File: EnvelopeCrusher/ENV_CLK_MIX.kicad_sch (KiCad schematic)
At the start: 12 parts, among them U14 TL072, U6 TL072

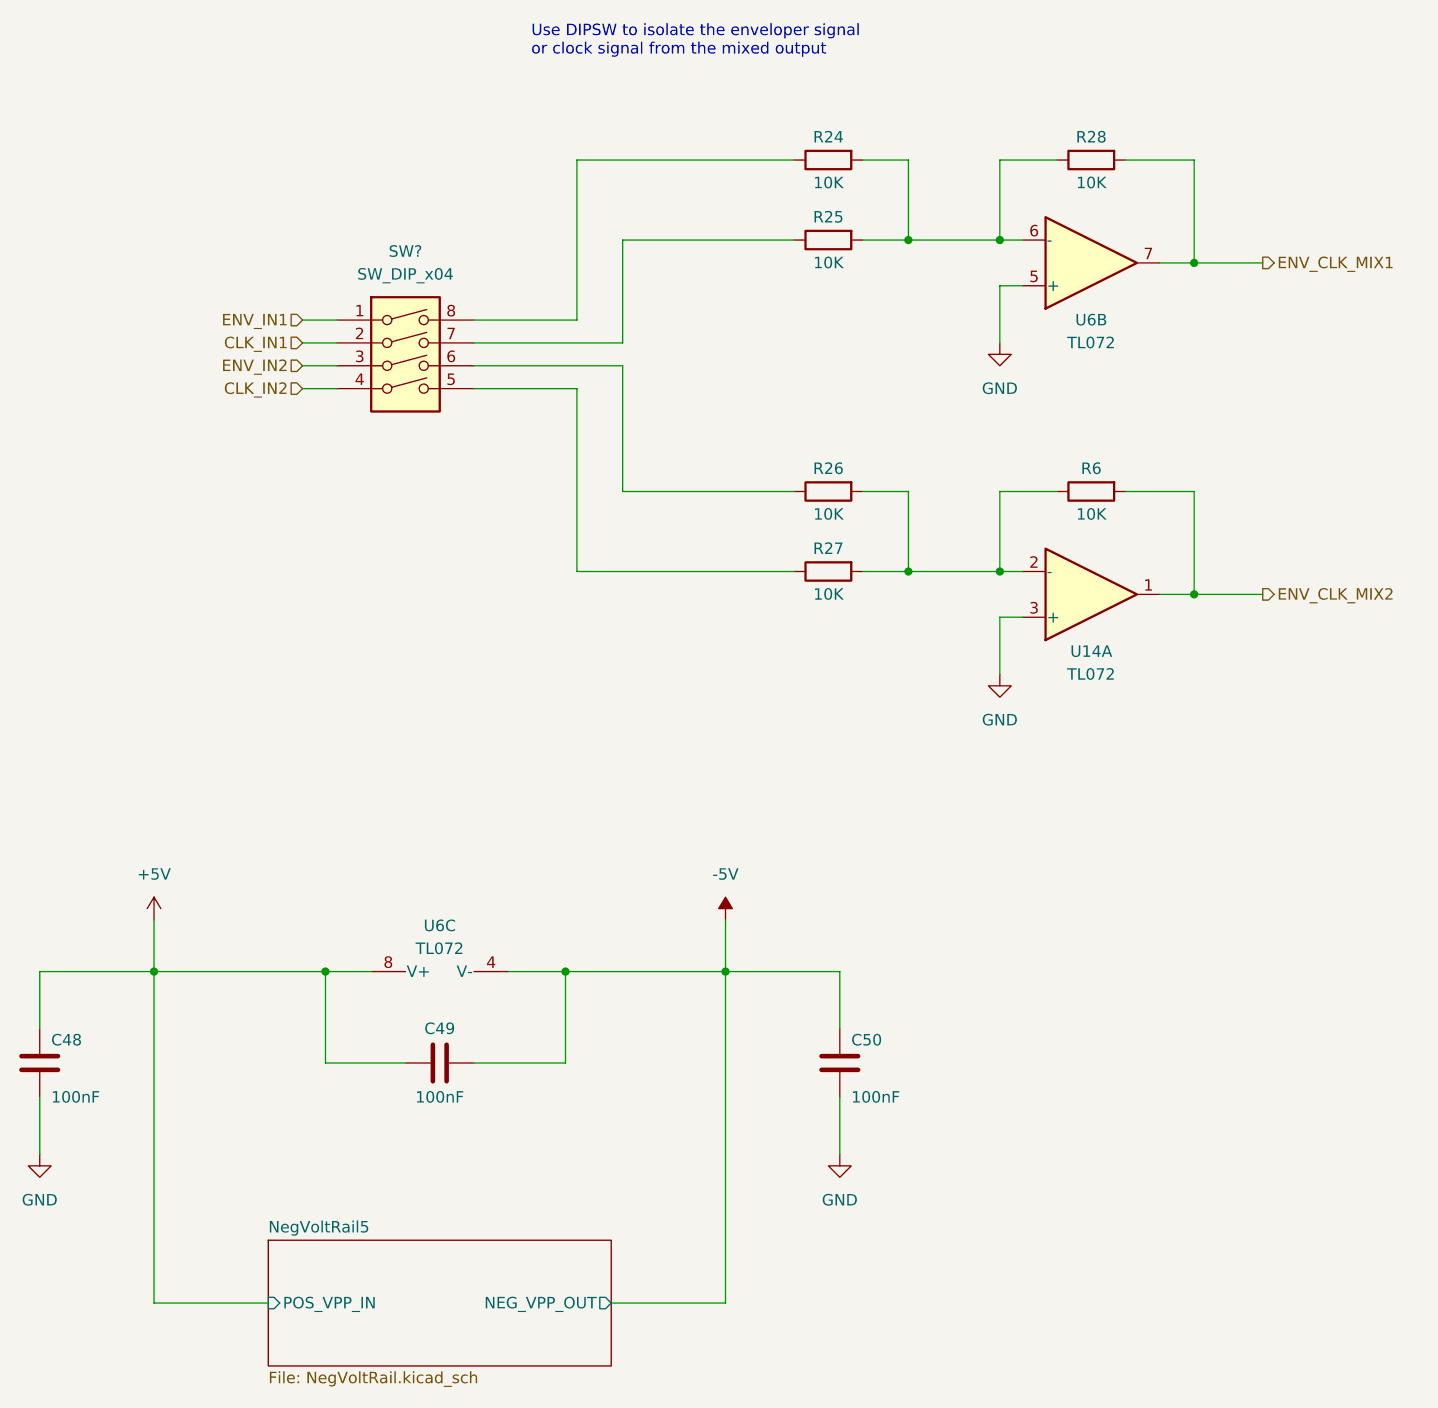
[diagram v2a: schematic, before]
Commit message: updated schematic
- Added values and comments to state-variable filter block
- Updated footprints
- Changed Dual Op Amp: TL072 to AM358
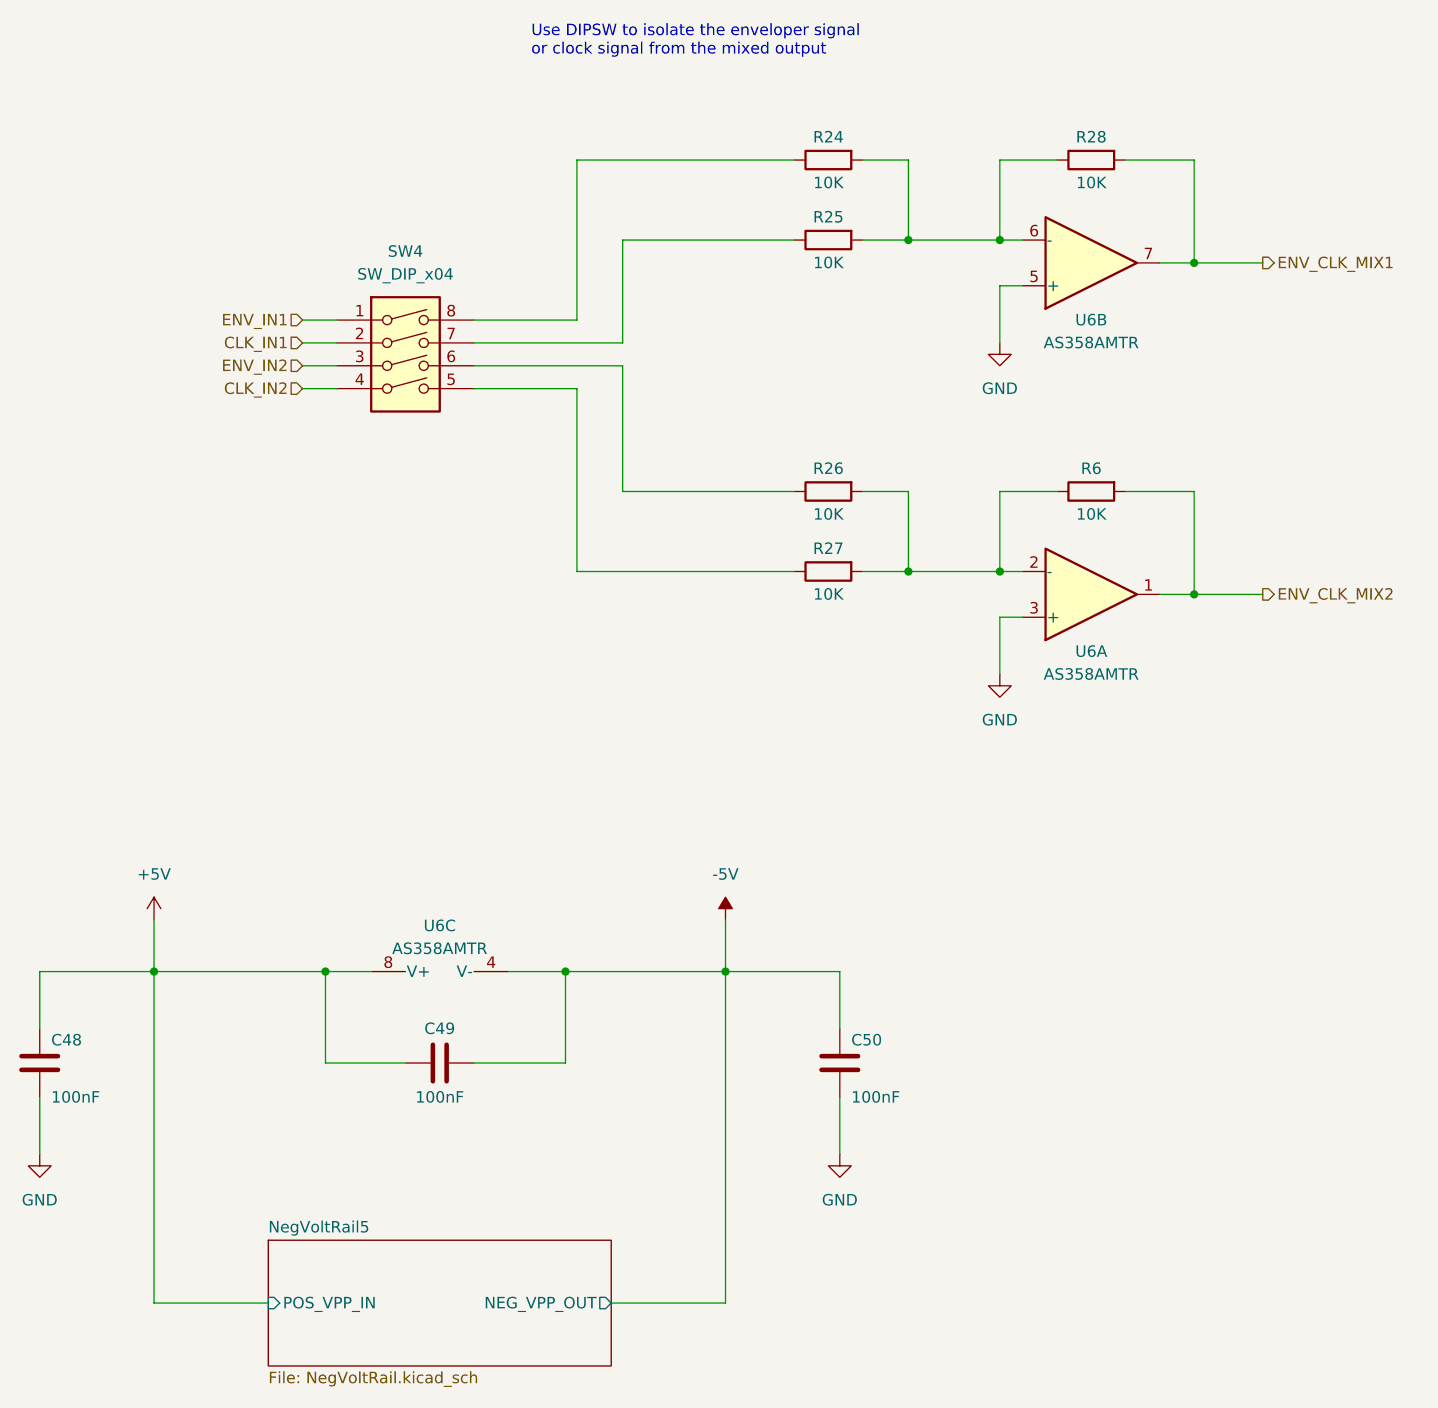
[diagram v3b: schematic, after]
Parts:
- U6: renamed from U14; value TL072 -> AS358AMTR; footprint (none) -> Package_SO:SOIC-8_3.9x4.9mm_P1.27mm
- U6: value TL072 -> AS358AMTR; footprint (none) -> Package_SO:SOIC-8_3.9x4.9mm_P1.27mm
- gave numbers to parts that had none: 1
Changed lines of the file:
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@@
   (symbol (lib_id "Switch:SW_DIP_x04") (at 72.39 72.39 0) (unit 1)
     (in_bom yes) (on_board yes) (fields_autoplaced)
-    (property "Reference" "SW?" (id 0) (at 72.39 59.69 0))
+    (property "Reference" "SW4" (id 0) (at 72.39 59.69 0))
     (property "Value" "SW_DIP_x04" (id 1) (at 72.39 62.23 0))
     (property "Footprint" "" (id 2) (at 72.39 72.39 0)
@@
   (symbol (lib_id "Amplifier_Operational:TL072") (at 148.59 97.79 0) (mirror x) (unit 1)
     (in_bom yes) (on_board yes)
-    (property "Reference" "U14" (id 0) (at 148.59 104.14 0))
-    (property "Value" "TL072" (id 1) (at 148.59 106.68 0))
-    (property "Footprint" "" (id 2) (at 148.59 97.79 0)
-      (effects (font (size 1.27 1.27)) hide)
-    )
-    (property "Datasheet" "http://www.ti.com/lit/ds/symlink/tl071.pdf" (id 3) (at 148.59 97.79 0)
+    (property "Reference" "U6" (id 0) (at 148.59 104.14 0))
+    (property "Value" "AS358AMTR" (id 1) (at 148.59 106.68 0))
+    (property "Footprint" "Package_SO:SOIC-8_3.9x4.9mm_P1.27mm" (id 2) (at 148.59 97.79 0)
+      (effects (font (size 1.27 1.27)) hide)
+    )
+    (property "Datasheet" "https://cdn.sparkfun.com/assets/8/4/9/e/1/DS-15946.pdf" (id 3) (at 148.59 97.79 0)
       (effects (font (size 1.27 1.27)) hide)
     )
@@
     (in_bom yes) (on_board yes)
     (property "Reference" "U6" (id 0) (at 148.59 67.31 0))
-    (property "Value" "TL072" (id 1) (at 148.59 69.85 0))
-    (property "Footprint" "" (id 2) (at 148.59 60.96 0)
-      (effects (font (size 1.27 1.27)) hide)
-    )
-    (property "Datasheet" "http://www.ti.com/lit/ds/symlink/tl071.pdf" (id 3) (at 148.59 60.96 0)
+    (property "Value" "AS358AMTR" (id 1) (at 148.59 69.85 0))
+    (property "Footprint" "Package_SO:SOIC-8_3.9x4.9mm_P1.27mm" (id 2) (at 148.59 60.96 0)
+      (effects (font (size 1.27 1.27)) hide)
+    )
+    (property "Datasheet" "https://cdn.sparkfun.com/assets/8/4/9/e/1/DS-15946.pdf" (id 3) (at 148.59 60.96 0)
       (effects (font (size 1.27 1.27)) hide)
     )
@@
     (in_bom yes) (on_board yes) (fields_autoplaced)
     (property "Reference" "U6" (id 0) (at 76.2 134.62 90))
-    (property "Value" "TL072" (id 1) (at 76.2 137.16 90))
-    (property "Footprint" "" (id 2) (at 76.2 137.16 0)
-      (effects (font (size 1.27 1.27)) hide)
-    )
-    (property "Datasheet" "http://www.ti.com/lit/ds/symlink/tl071.pdf" (id 3) (at 76.2 137.16 0)
-      (effects (font (size 1.27 1.27)) hide)
-    )
+    (property "Value" "AS358AMTR" (id 1) (at 76.2 137.16 90))
+    (property "Footprint" "Package_SO:SOIC-8_3.9x4.9mm_P1.27mm" (id 2) (at 76.2 137.16 0)
+      (effects (font (size 1.27 1.27)) hide)
+    )
+    (property "Datasheet" "https://cdn.sparkfun.com/assets/8/4/9/e/1/DS-15946.pdf" (id 3) (at 76.2 137.16 0)
+      (effects (font (size 1.27 1.27)) hide)
+    )

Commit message: started layout
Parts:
- SW4: footprint (none) -> Button_Switch_THT:SW_DIP_SPSTx04_Slide_6.7x11.72mm_W7.62mm_P2.54mm_LowProfile
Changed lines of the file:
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@@
     (property "Reference" "SW4" (id 0) (at 72.39 59.69 0))
     (property "Value" "SW_DIP_x04" (id 1) (at 72.39 62.23 0))
-    (property "Footprint" "" (id 2) (at 72.39 72.39 0)
+    (property "Footprint" "Button_Switch_THT:SW_DIP_SPSTx04_Slide_6.7x11.72mm_W7.62mm_P2.54mm_LowProfile" (id 2) (at 72.39 72.39 0)
       (effects (font (size 1.27 1.27)) hide)
     )

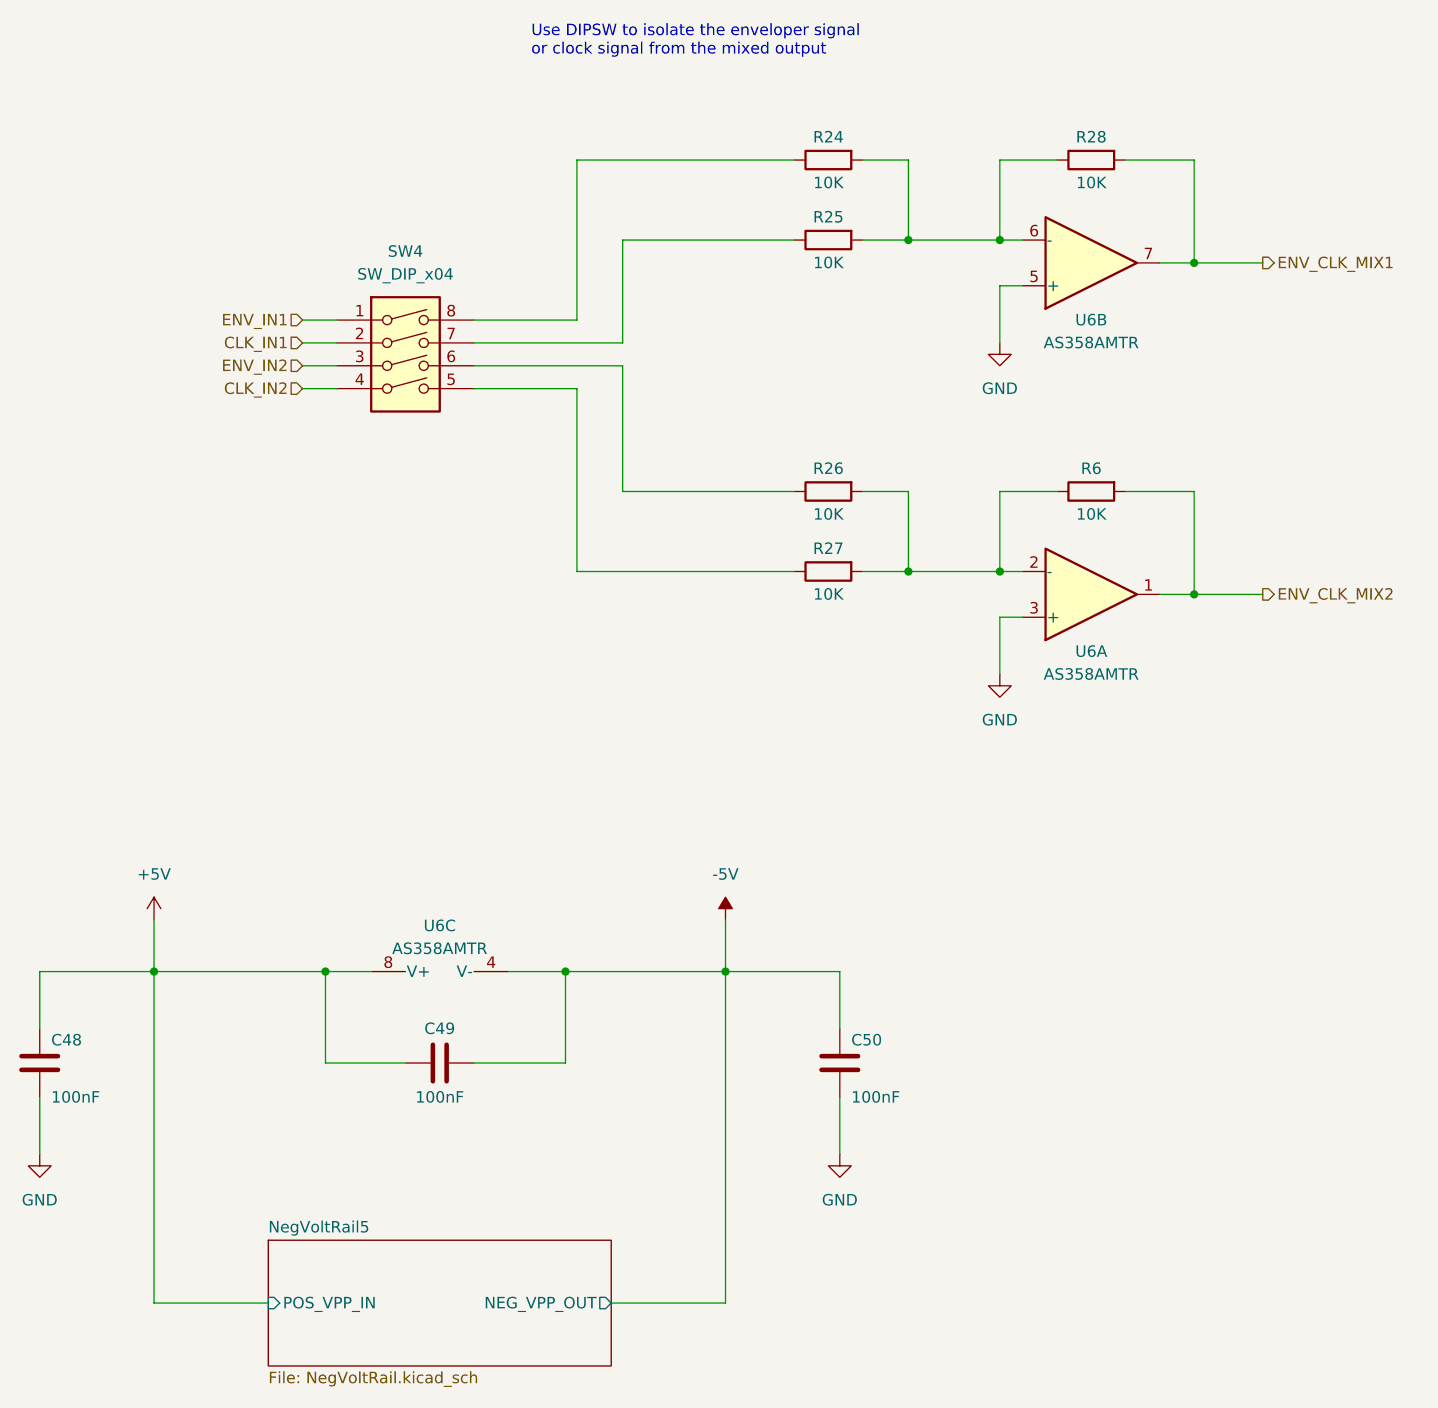
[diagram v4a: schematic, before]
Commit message: organised layout into functional blocks
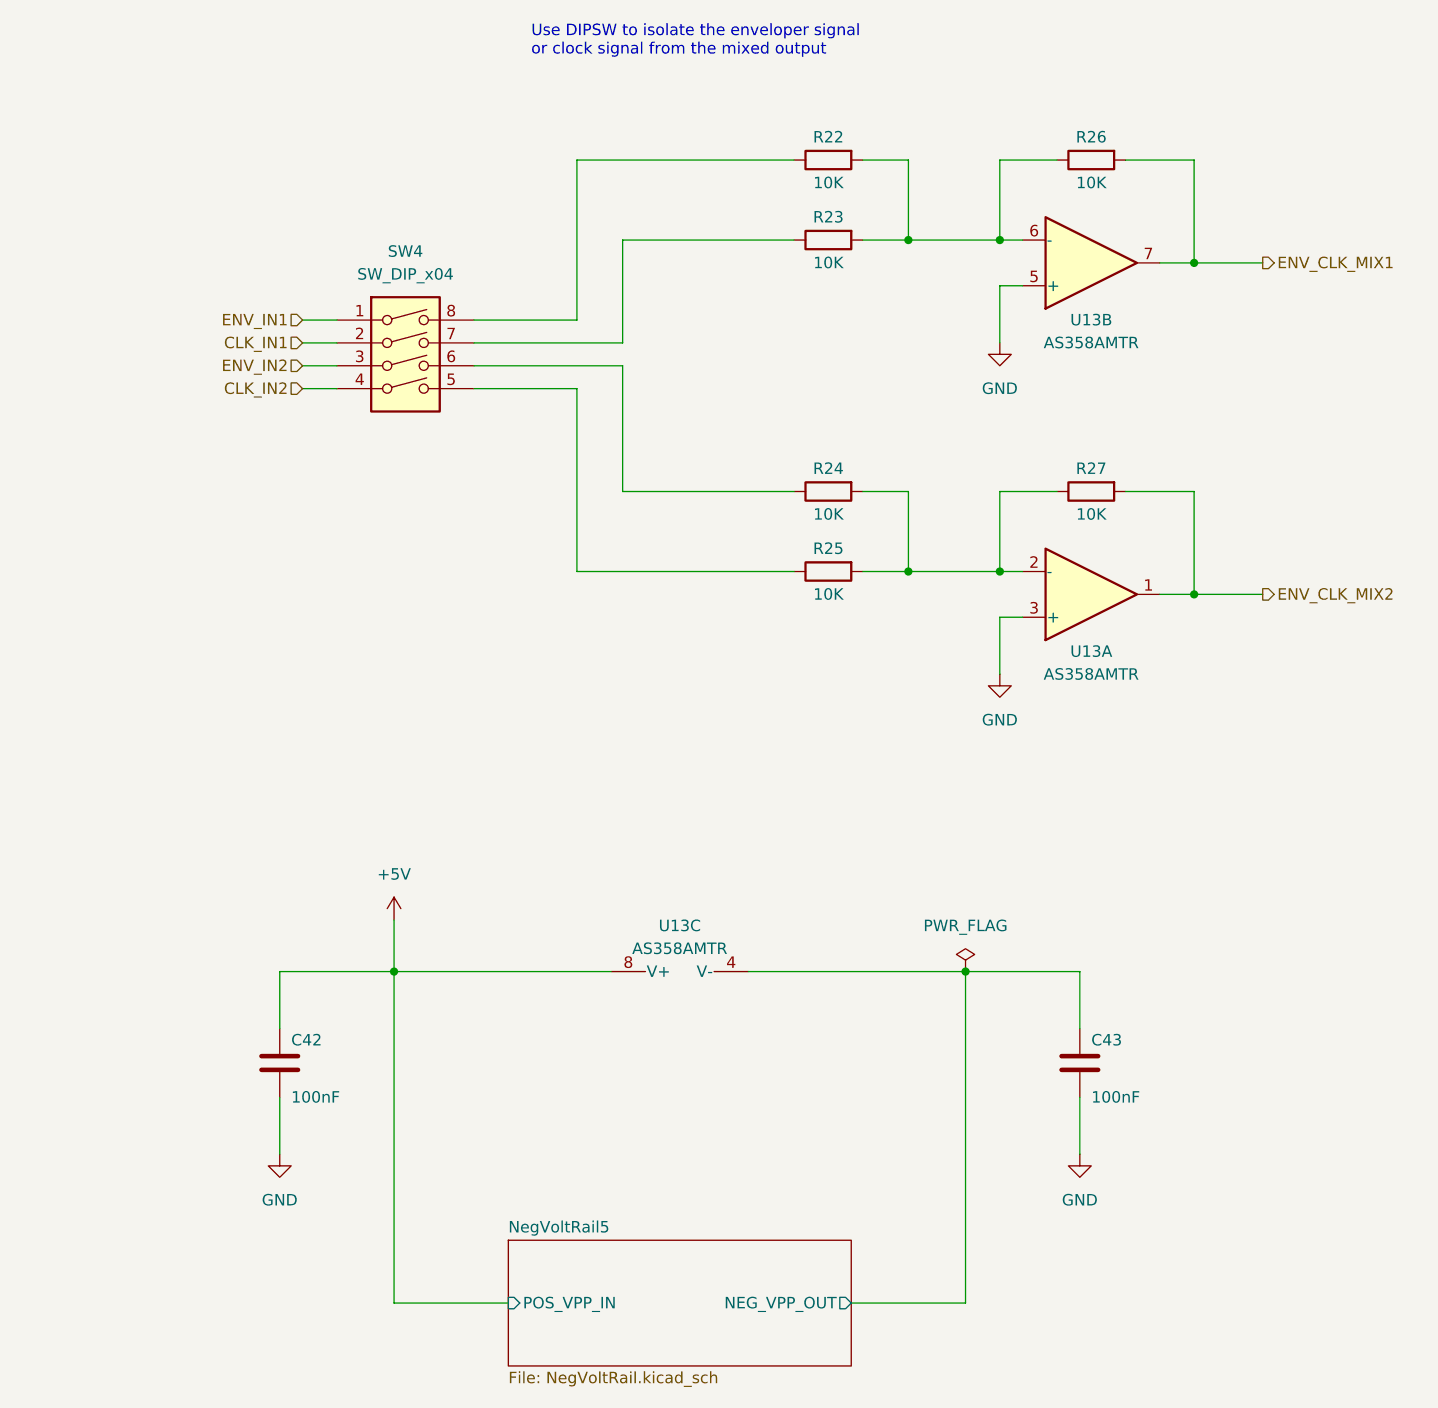
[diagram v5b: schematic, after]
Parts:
- removed C49: 100nF, Capacitor_SMD:C_0805_2012Metric_Pad1.18x1.45mm_HandSolder, symbol Device:C
- renumbered C48 to C42, C50 to C43, R24 to R22, R25 to R23, R26 to R24, R27 to R25, R28 to R26, R6 to R27, U6 to U13
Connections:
- net -5V renamed NegVoltRail5/NEG_VPP_OUT
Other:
- moved on the sheet: C42, C43, U13C
